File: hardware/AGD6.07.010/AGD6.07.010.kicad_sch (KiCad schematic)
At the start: 0 parts

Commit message: Draw full AGD6.07.010 schematic per integrated_avionics_board spec
All ten sheets now carry components: 14S input with hot-swap and power
monitor, 12/5/3.3 V rails and a separate 12 V AI channel with soft-start
and current telemetry, Pixhawk connectors, CAN1/CAN2 hub with chokes,
ESD and switchable termination, sensor conditioning, SIYI and radar,
AI interface and watchdog, protected 12 V switches with diagnostics,
fan/heater control, cameras and Ethernet. Open choices are recorded in
DECISIONS.md; datasheet-dependent values are flagged CHECK_DATASHEET.

ERC: no errors. All 752 intended pin connections match the KiCad netlist.

Co-Authored-By: Claude Opus 5.5 <noreply@anthropic.com>
Claude-Session: https://claude.ai/code/session_01Qk7uTKdi6YbndB9fGuguYV
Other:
- sheet CAMERAS ports: added CAM_TRIG; removed none
- sheet CAN_AND_SENSORS ports: added ADC_LEVEL, ADC_PRESS, CAN1_H, CAN1_L, CAN2_H, CAN2_L, ESC_PWM1, ESC_PWM2, ESC_PWM3, ESC_PWM4, ESC_PWM5, ESC_PWM6, FLOW_CAP; removed none
- sheet FLIGHT_CONTROL_IO ports: added ADC_LEVEL, ADC_PRESS, AI_RX, AI_TX, CAM_TRIG, CAN1_H, CAN1_L, CAN2_H, CAN2_L, ESC_PWM1, ESC_PWM2, ESC_PWM3, ESC_PWM4, ESC_PWM5, ESC_PWM6, FAN_CTL, FLOW_CAP, HEATER_CTL, I2C_SCL, I2C_SDA, LIGHTS_CTL, MAV_PX_RX, MAV_PX_TX, PUMP_PWM, RADAR_PX_RX, RADAR_PX_TX, SBUS, VALVE1_CTL, VALVE2_CTL; removed none
- sheet LOAD_SWITCHES_12V ports: added FAN_CTL, HEATER_CTL, I2C_SCL, I2C_SDA, LIGHTS_CTL, PUMP_PWM, TEMP_ALERT_N, VALVE1_CTL, VALVE2_CTL; removed none
- sheet POWER_CONVERSION ports: added AI_PWR_EN, I2C_SCL, I2C_SDA, VIN_PROT; removed none
- sheet POWER_INPUT_14S ports: added I2C_SCL, I2C_SDA, VIN_PROT; removed none
- sheet RC_AND_TELEMETRY ports: added GNSS_PPS, MAV_PX_RX, MAV_PX_TX, RADAR_PX_RX, RADAR_PX_TX, SBUS; removed none
- note added: "АГД6.07.010 — центральная плата авионики гексакоптера X6. Rev 0.2. DATA_REQUIRED / NOT_FOR_MANUFACTURE / NOT_FOR_FLIGHT. ТЗ: integrated_avionics_board.md. Решения: DECISIONS.md. Вне платы: BMS, PDB 14S и предохранители 250 A / лучей, power module, ESC, насос, FTS."
- note removed: "АГД6.07.010 — центральная плата авионики гексакоптера X6. DATA_REQUIRED / NOT_FOR_MANUFACTURE / NOT_FOR_FLIGHT. Вне платы: BMS, силовая шина 14S (PDB), предохранители 250 A / лучей, power module Mauch, ESC, насос, FTS."

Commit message: AGD6.07.010 rev 0.3: design review fixes and bring-up plan
Design review (DESIGN_REVIEW.md) with fixes applied to the schematic:
INA228 input RC filters, 12 V bus current monitor (INA228 0x45),
BTS5030 diagnostic scaling with clamp diodes, flow input level fix,
CAN1 changed from star to daisy chain with on-board terminator, AI
shutdown request, board buzzer, series resistors and ESD on external
I2C probes. Connectors merged so every connector sits on a board edge.
Adds calculations.md (power, IPC-2221 widths, hot-swap, thermal, ADC
scaling, CAN, clearances) and BRINGUP.md (step-by-step test plan).
ERC: no errors; all 820 intended pin connections verified. Board is
re-placed; routing in progress.

Co-Authored-By: Claude Opus 5.5 <noreply@anthropic.com>
Claude-Session: https://claude.ai/code/session_01Qk7uTKdi6YbndB9fGuguYV
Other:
- sheet AI_COMPUTE_INTERFACE ports: added AI_SHDN_REQ; removed none
- sheet CAMERAS ports: added none; removed CAM_TRIG
- sheet FLIGHT_CONTROL_IO ports: added AI_SHDN_REQ, BUZZER_CTL; removed none
- sheet LOAD_SWITCHES_12V ports: added BUZZER_CTL, CAM_TRIG; removed none

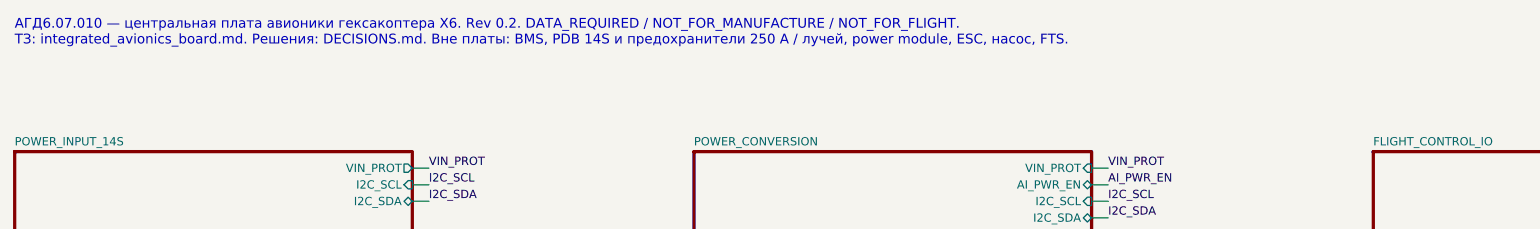
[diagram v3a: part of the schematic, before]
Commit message: AGD6.07.010 rev 0.4 (WIP): 3x TRACO THL40 DC/DC, split 12 V bus, SwitchBlox Ethernet, fixed LM5069 UVLO/OVLO, computed hot-swap values, PX4 firmware notes; board re-placed, routing in progress
Co-Authored-By: Claude Opus 5.5 <noreply@anthropic.com>
Claude-Session: https://claude.ai/code/session_01Qk7uTKdi6YbndB9fGuguYV
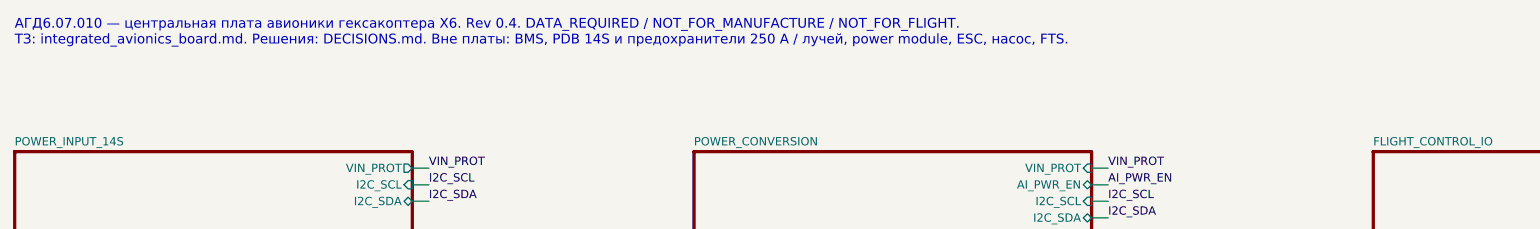
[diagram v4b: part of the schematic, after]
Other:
- note added: "АГД6.07.010 — центральная плата авионики гексакоптера X6. Rev 0.4. DATA_REQUIRED / NOT_FOR_MANUFACTURE / NOT_FOR_FLIGHT. ТЗ: integrated_avionics_board.md. Решения: DECISIONS.md. Вне платы: BMS, PDB 14S и предохранители 250 A / лучей, power module, ESC, насос, FTS."
- note removed: "АГД6.07.010 — центральная плата авионики гексакоптера X6. Rev 0.2. DATA_REQUIRED / NOT_FOR_MANUFACTURE / NOT_FOR_FLIGHT. ТЗ: integrated_avionics_board.md. Решения: DECISIONS.md. Вне платы: BMS, PDB 14S и предохранители 250 A / лучей, power module, ESC, насос, FTS."
